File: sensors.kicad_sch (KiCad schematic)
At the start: 55 parts, among them IC1 TCA9548ARGERQ1, IC2 SGP40-D-R4, IC3 SGP40-D-R4, IC4 SGP40-D-R4, IC6 SGP40-D-R4, U3 BMP581, U4 BMP581, U5 BMP581, U6 BMP581

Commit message: fix: missing footprints
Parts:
- C10, C11, C12, C13, C14, C7, C8, C9: footprint (none) -> Capacitor_SMD:C_0603_1608Metric
- IC1: footprint QFN50P400X400X100-25N-D -> Local:QFN50P400X400X100-25N-D
- IC2, IC3, IC4, IC6: footprint SON80P244X244X95-7N -> Local:SON80P244X244X95-7N
- JP1, JP2, JP3, JP4, JP5, JP6, JP7: footprint (none) -> Jumper:SolderJumper-3_P1.3mm_Open_RoundedPad1.0x1.5mm
- R1, R10, R12, R14, R15, R16, R17, R18, R19, R2, R20, R21, R22, R23, R24, R25, R26, R3, R4, R5, R6, R7: footprint (none) -> Resistor_SMD:R_0603_1608Metric
- U3, U4, U5, U6: footprint BMP581 -> Local:BMP581
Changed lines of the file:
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@@
 			)
 		)
-		(property "Footprint" "SON80P244X244X95-7N"
+		(property "Footprint" "Local:SON80P244X244X95-7N"
 			(at 246.38 148.26 0)
 			(effects
@@
 			)
 		)
-		(property "Footprint" ""
+		(property "Footprint" "Resistor_SMD:R_0603_1608Metric"
 			(at 92.202 52.07 90)
 			(effects
@@
 			)
 		)
-		(property "Footprint" ""
+		(property "Footprint" "Resistor_SMD:R_0603_1608Metric"
 			(at 342.392 97.79 90)
 			(effects
@@
 			)
 		)
-		(property "Footprint" ""
+		(property "Footprint" "Resistor_SMD:R_0603_1608Metric"
 			(at 197.612 100.33 90)
 			(effects
@@
 			)
 		)
-		(property "Footprint" "BMP581"
+		(property "Footprint" "Local:BMP581"
 			(at 130.81 270.18 0)
 			(effects
@@
 			)
 		)
-		(property "Footprint" ""
+		(property "Footprint" "Resistor_SMD:R_0603_1608Metric"
 			(at 252.222 46.99 90)
 			(effects
@@
 			)
 		)
-		(property "Footprint" "BMP581"
+		(property "Footprint" "Local:BMP581"
 			(at 130.81 145.72 0)
 			(effects
@@
 			)
 		)
-		(property "Footprint" ""
+		(property "Footprint" "Jumper:SolderJumper-3_P1.3mm_Open_RoundedPad1.0x1.5mm"
 			(at 314.96 191.77 0)
 			(effects
@@
 			)
 		)
-		(property "Footprint" ""
+		(property "Footprint" "Capacitor_SMD:C_0603_1608Metric"
 			(at 112.7252 166.37 0)
 			(effects
@@
 			)
 		)
-		(property "Footprint" ""
+		(property "Footprint" "Resistor_SMD:R_0603_1608Metric"
 			(at 211.582 87.63 90)
 			(effects
@@
 			)
 		)
-		(property "Footprint" ""
+		(property "Footprint" "Resistor_SMD:R_0603_1608Metric"
 			(at 97.282 114.3 90)
 			(effects
@@
 			)
 		)
-		(property "Footprint" ""
+		(property "Footprint" "Capacitor_SMD:C_0603_1608Metric"
 			(at 127.9652 104.14 0)
 			(effects
@@
 			)
 		)
-		(property "Footprint" ""
+		(property "Footprint" "Resistor_SMD:R_0603_1608Metric"
 			(at 211.582 40.64 90)
 			(effects
@@
 			)
 		)
-		(property "Footprint" ""
+		(property "Footprint" "Capacitor_SMD:C_0603_1608Metric"
 			(at 112.7252 41.91 0)
 			(effects
@@
 			)
 		)
-		(property "Footprint" ""
+		(property "Footprint" "Resistor_SMD:R_0603_1608Metric"
 			(at 92.202 238.76 90)
 			(effects
@@
 			)
 		)
-		(property "Footprint" ""
+		(property "Footprint" "Capacitor_SMD:C_0603_1608Metric"
 			(at 127.9652 228.6 0)
 			(effects
@@
 			)
 		)
-		(property "Footprint" ""
+		(property "Footprint" "Capacitor_SMD:C_0603_1608Metric"
 			(at 112.7252 104.14 0)
 			(effects
@@
 			)
 		)
-		(property "Footprint" ""
+		(property "Footprint" "Resistor_SMD:R_0603_1608Metric"
 			(at 97.282 176.53 90)
 			(effects
@@
 			)
 		)
-		(property "Footprint" ""
+		(property "Footprint" "Jumper:SolderJumper-3_P1.3mm_Open_RoundedPad1.0x1.5mm"
 			(at 142.24 250.19 0)
 			(effects
@@
 			)
 		)
-		(property "Footprint" ""
+		(property "Footprint" "Resistor_SMD:R_0603_1608Metric"
 			(at 352.552 97.79 90)
 			(effects
@@
 			)
 		)
-		(property "Footprint" ""
+		(property "Footprint" "Jumper:SolderJumper-3_P1.3mm_Open_RoundedPad1.0x1.5mm"
 			(at 331.47 191.77 0)
 			(effects
@@
 			)
 		)
-		(property "Footprint" ""
+		(property "Footprint" "Jumper:SolderJumper-3_P1.3mm_Open_RoundedPad1.0x1.5mm"
 			(at 142.24 187.96 0)
 			(effects
@@
 			)
 		)
-		(property "Footprint" ""
+		(property "Footprint" "Resistor_SMD:R_0603_1608Metric"
 			(at 252.222 144.78 90)
 			(effects
@@
 			)
 		)
-		(property "Footprint" ""
+		(property "Footprint" "Capacitor_SMD:C_0603_1608Metric"
 			(at 127.9652 41.91 0)
 			(effects
@@
 			)
 		)
-		(property "Footprint" ""
+		(property "Footprint" "Jumper:SolderJumper-3_P1.3mm_Open_RoundedPad1.0x1.5mm"
 			(at 142.24 125.73 0)
 			(effects
@@
 			)
 		)
-		(property "Footprint" "QFN50P400X400X100-25N-D"
+		(property "Footprint" "Local:QFN50P400X400X100-25N-D"
 			(at 342.9 210.49 0)
 			(effects
@@
 			)
 		)
-		(property "Footprint" ""
+		(property "Footprint" "Resistor_SMD:R_0603_1608Metric"
 			(at 211.582 138.43 90)
 			(effects
@@
 			)
 		)
-		(property "Footprint" "SON80P244X244X95-7N"
+		(property "Footprint" "Local:SON80P244X244X95-7N"
 			(at 246.38 246.05 0)
 			(effects
@@
 			)
 		)
-		(property "Footprint" ""
+		(property "Footprint" "Resistor_SMD:R_0603_1608Metric"
 			(at 197.612 53.34 90)
 			(effects
@@
 			)
 		)
-		(property "Footprint" ""
+		(property "Footprint" "Capacitor_SMD:C_0603_1608Metric"
 			(at 112.7252 228.6 0)
 			(effects
@@
 			)
 		)
-		(property "Footprint" ""
+		(property "Footprint" "Resistor_SMD:R_0603_1608Metric"
 			(at 252.222 93.98 90)
 			(effects
@@
 			)
 		)
-		(property "Footprint" ""
+		(property "Footprint" "Resistor_SMD:R_0603_1608Metric"
 			(at 252.222 198.12 90)
 			(effects
@@
 			)
 		)
-		(property "Footprint" ""
+		(property "Footprint" "Resistor_SMD:R_0603_1608Metric"
 			(at 211.582 191.77 90)
 			(effects
@@
 			)
 		)
-		(property "Footprint" ""
+		(property "Footprint" "Jumper:SolderJumper-3_P1.3mm_Open_RoundedPad1.0x1.5mm"
 			(at 347.98 191.77 0)
 			(effects
@@
 			)
 		)
-		(property "Footprint" ""
+		(property "Footprint" "Resistor_SMD:R_0603_1608Metric"
 			(at 197.612 151.13 90)
 			(effects
@@
 			)
 		)
-		(property "Footprint" ""
+		(property "Footprint" "Capacitor_SMD:C_0603_1608Metric"
 			(at 127.9652 166.37 0)
 			(effects
@@
 			)
 		)
-		(property "Footprint" ""
+		(property "Footprint" "Resistor_SMD:R_0603_1608Metric"
 			(at 197.612 204.47 90)
 			(effects
@@
 			)
 		)
-		(property "Footprint" ""
+		(property "Footprint" "Resistor_SMD:R_0603_1608Metric"
 			(at 97.282 52.07 90)
 			(effects
@@
 			)
 		)
-		(property "Footprint" "BMP581"
+		(property "Footprint" "Local:BMP581"
 			(at 130.81 332.41 0)
 			(effects
@@
 			)
 		)
-		(property "Footprint" ""
+		(property "Footprint" "Resistor_SMD:R_0603_1608Metric"
 			(at 92.202 176.53 90)
 			(effects
@@
 			)
 		)
-		(property "Footprint" ""
+		(property "Footprint" "Resistor_SMD:R_0603_1608Metric"
 			(at 92.202 114.3 90)
 			(effects
@@
 			)
 		)
-		(property "Footprint" "SON80P244X244X95-7N"
+		(property "Footprint" "Local:SON80P244X244X95-7N"
 			(at 246.38 299.39 0)
 			(effects
@@
 			)
 		)
-		(property "Footprint" ""
+		(property "Footprint" "Jumper:SolderJumper-3_P1.3mm_Open_RoundedPad1.0x1.5mm"
 			(at 142.24 63.5 0)
 			(effects
@@
 			)
 		)
-		(property "Footprint" ""
+		(property "Footprint" "Resistor_SMD:R_0603_1608Metric"
 			(at 97.282 238.76 90)
 			(effects
@@
 			)
 		)
-		(property "Footprint" "BMP581"
+		(property "Footprint" "Local:BMP581"
 			(at 130.81 207.95 0)
 			(effects
@@
 			)
 		)
-		(property "Footprint" "SON80P244X244X95-7N"
+		(property "Footprint" "Local:SON80P244X244X95-7N"
 			(at 246.38 195.25 0)
 			(effects

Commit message: fix: missing footprints
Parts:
- C15, C16, C18, C20, C21, C22, C4, C5, C6: footprint (none) -> Capacitor_SMD:C_0603_1608Metric
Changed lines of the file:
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@@
 			)
 		)
-		(property "Footprint" ""
+		(property "Footprint" "Capacitor_SMD:C_0603_1608Metric"
 			(at 262.5852 64.77 0)
 			(effects
@@
 			)
 		)
-		(property "Footprint" ""
+		(property "Footprint" "Capacitor_SMD:C_0603_1608Metric"
 			(at 329.8952 95.25 0)
 			(effects
@@
 			)
 		)
-		(property "Footprint" ""
+		(property "Footprint" "Capacitor_SMD:C_0603_1608Metric"
 			(at 214.3252 152.4 0)
 			(effects
@@
 			)
 		)
-		(property "Footprint" ""
+		(property "Footprint" "Capacitor_SMD:C_0603_1608Metric"
 			(at 262.5852 111.76 0)
 			(effects
@@
 			)
 		)
-		(property "Footprint" ""
+		(property "Footprint" "Capacitor_SMD:C_0603_1608Metric"
 			(at 214.3252 101.6 0)
 			(effects
@@
 			)
 		)
-		(property "Footprint" ""
+		(property "Footprint" "Capacitor_SMD:C_0603_1608Metric"
 			(at 262.5852 162.56 0)
 			(effects
@@
 			)
 		)
-		(property "Footprint" ""
+		(property "Footprint" "Capacitor_SMD:C_0603_1608Metric"
 			(at 262.5852 215.9 0)
 			(effects
@@
 			)
 		)
-		(property "Footprint" ""
+		(property "Footprint" "Capacitor_SMD:C_0603_1608Metric"
 			(at 214.3252 205.74 0)
 			(effects
@@
 			)
 		)
-		(property "Footprint" ""
+		(property "Footprint" "Capacitor_SMD:C_0603_1608Metric"
 			(at 214.3252 54.61 0)
 			(effects

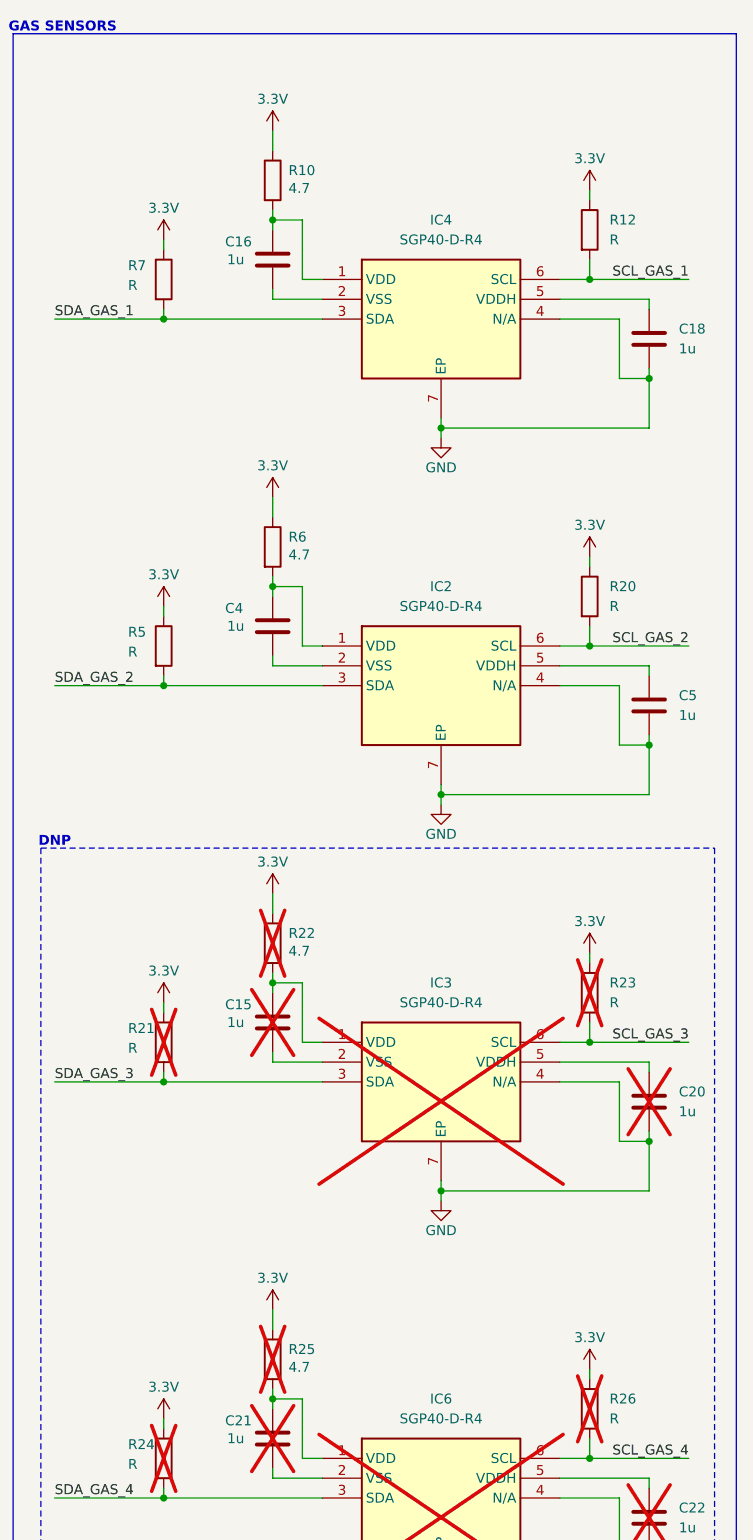
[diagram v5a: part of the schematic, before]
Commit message: fix: fllags and footprints
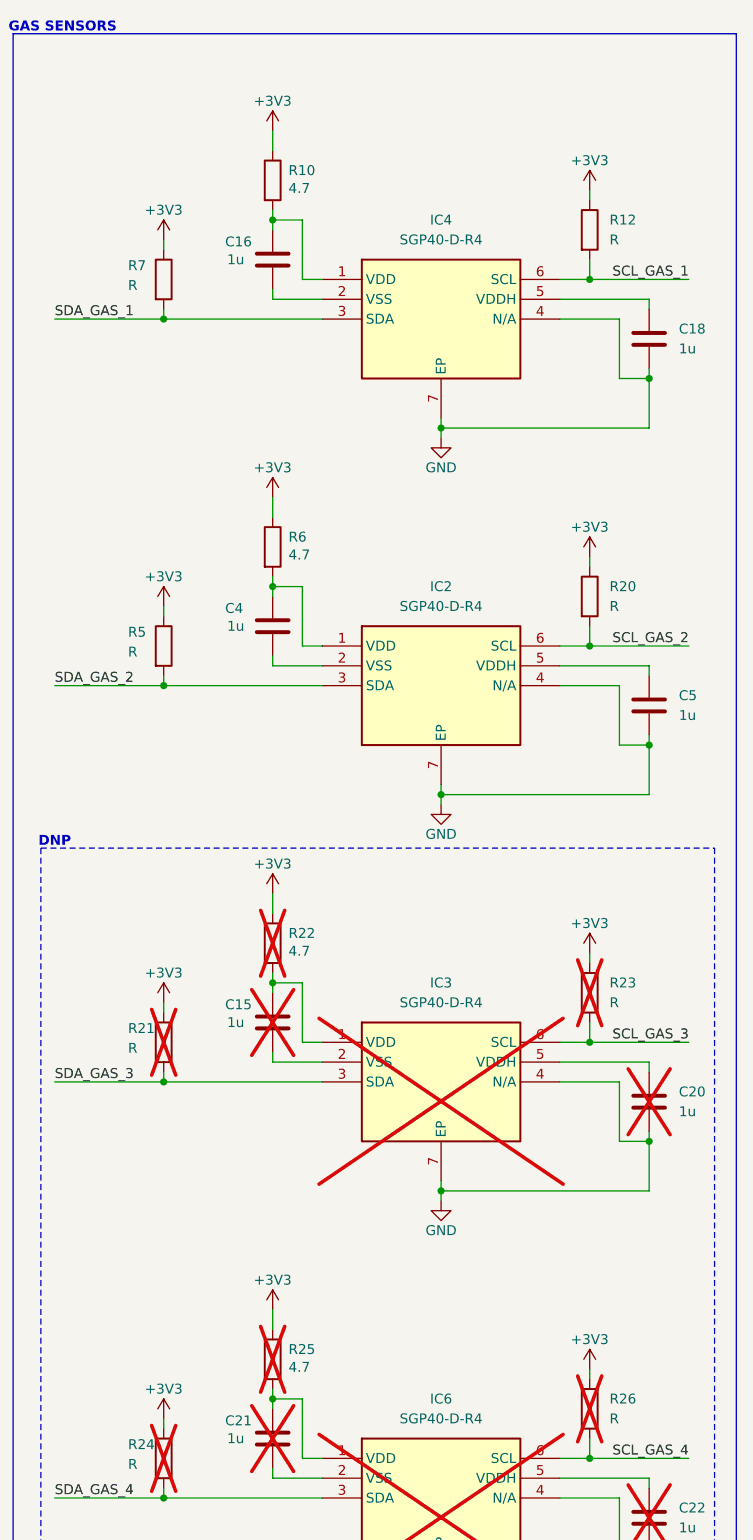
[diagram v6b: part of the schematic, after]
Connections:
- net 3.3V is gone; now on net +3V3: R10.1, R12.1, R20.1, R21.1, R22.1, R23.1, R24.1, R25.1, R26.1, R5.1, R6.1, R7.1

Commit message: feat: first sensors couple connected
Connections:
- net SCK_PRESS_1: no longer IC1.11 (SC4)
- net SCK_PRESS_4: now also IC1.8 (SC3); no longer IC1.17 (SC7)
- net SCL_GAS_4: now also IC1.11 (SC4); no longer IC1.8 (SC3)
- net SDA_GAS_4: now also IC1.10 (SD4); no longer IC1.7 (SD3)
- net SDA_PRESS_1: no longer IC1.10 (SD4)
- net SDA_PRESS_4: now also IC1.7 (SD3); no longer IC1.16 (SD7)

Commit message: feat: first pcb draft completed
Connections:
- net SCK_PRESS_1: now also IC1.8 (SC3)
- net SCK_PRESS_2: now also IC1.3 (SD1); no longer IC1.13 (SC5)
- net SCK_PRESS_4: now also IC1.11 (SC4); no longer IC1.8 (SC3)
- net SCL_GAS_2: now also IC1.6 (SC2); no longer IC1.4 (SC1)
- net SCL_GAS_3: now also IC1.17 (SC7); no longer IC1.6 (SC2)
- net SCL_GAS_4: now also IC1.13 (SC5); no longer IC1.11 (SC4)
- net SDA_GAS_2: now also IC1.5 (SD2); no longer IC1.3 (SD1)
- net SDA_GAS_3: now also IC1.16 (SD7); no longer IC1.5 (SD2)
- net SDA_GAS_4: now also IC1.12 (SD5); no longer IC1.10 (SD4)
- net SDA_PRESS_1: now also IC1.7 (SD3)
- net SDA_PRESS_2: now also IC1.4 (SC1); no longer IC1.12 (SD5)
- net SDA_PRESS_4: now also IC1.10 (SD4); no longer IC1.7 (SD3)
